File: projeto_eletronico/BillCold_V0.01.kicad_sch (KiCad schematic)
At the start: 36 parts, among them J1 USB_B, U1 ESP32-S3, U2 AMS1117, U3 W25Q128JVSIQ, X1 OSCILADOR-3225

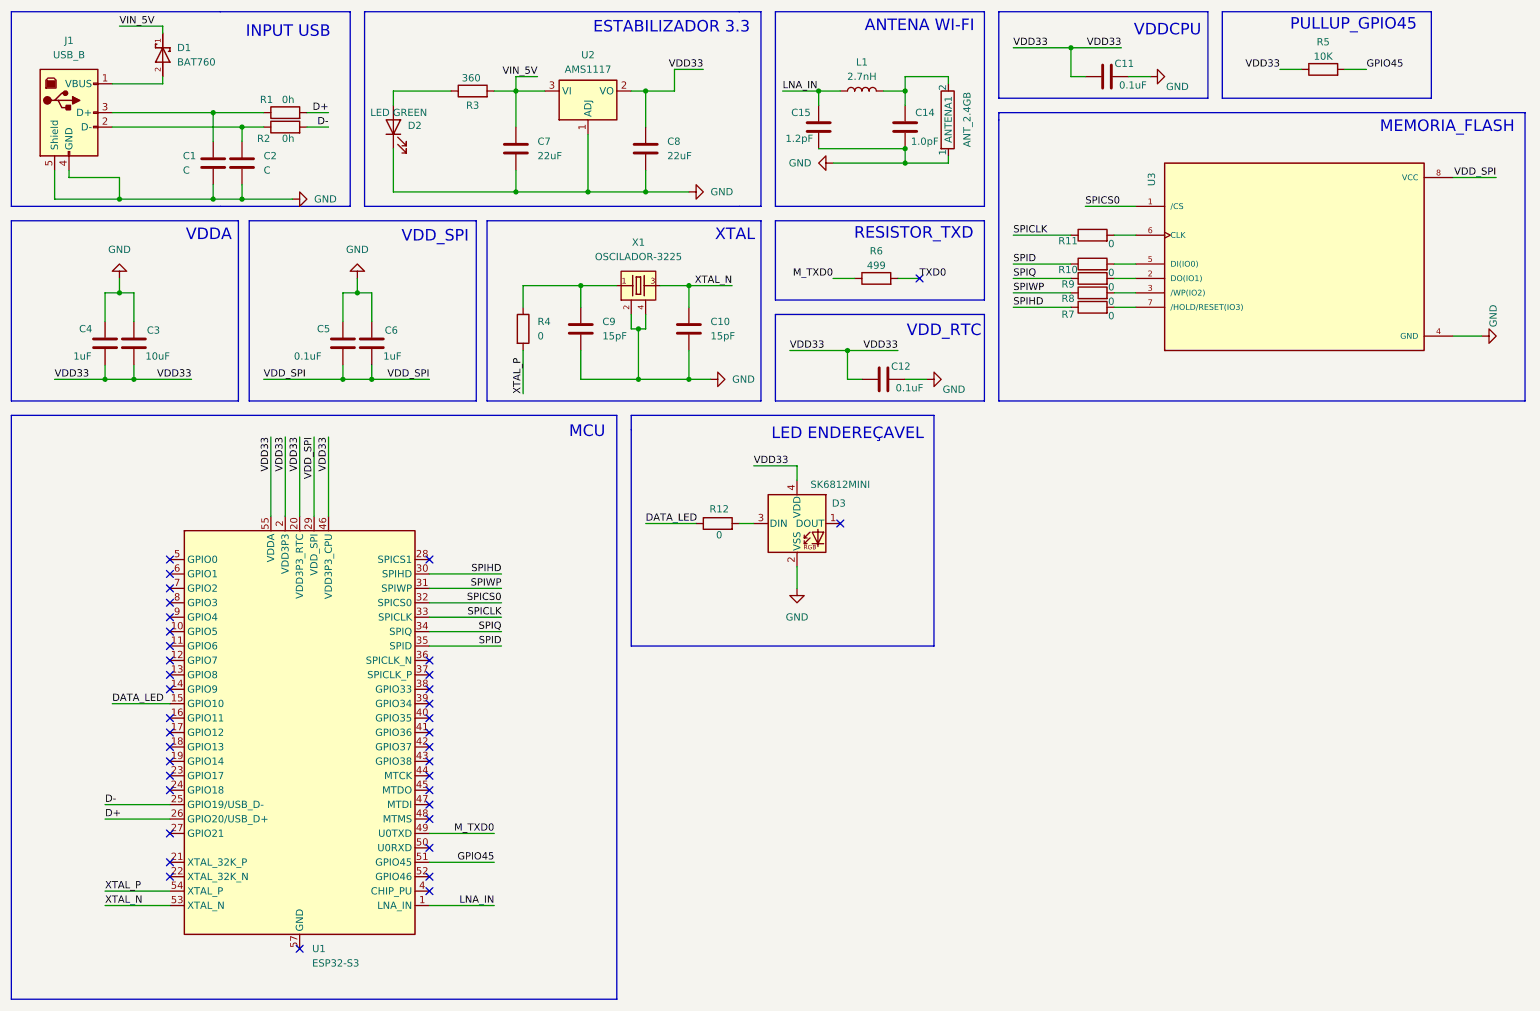
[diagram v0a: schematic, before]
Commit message: Iniciando o roteamento das trilhas da PCB
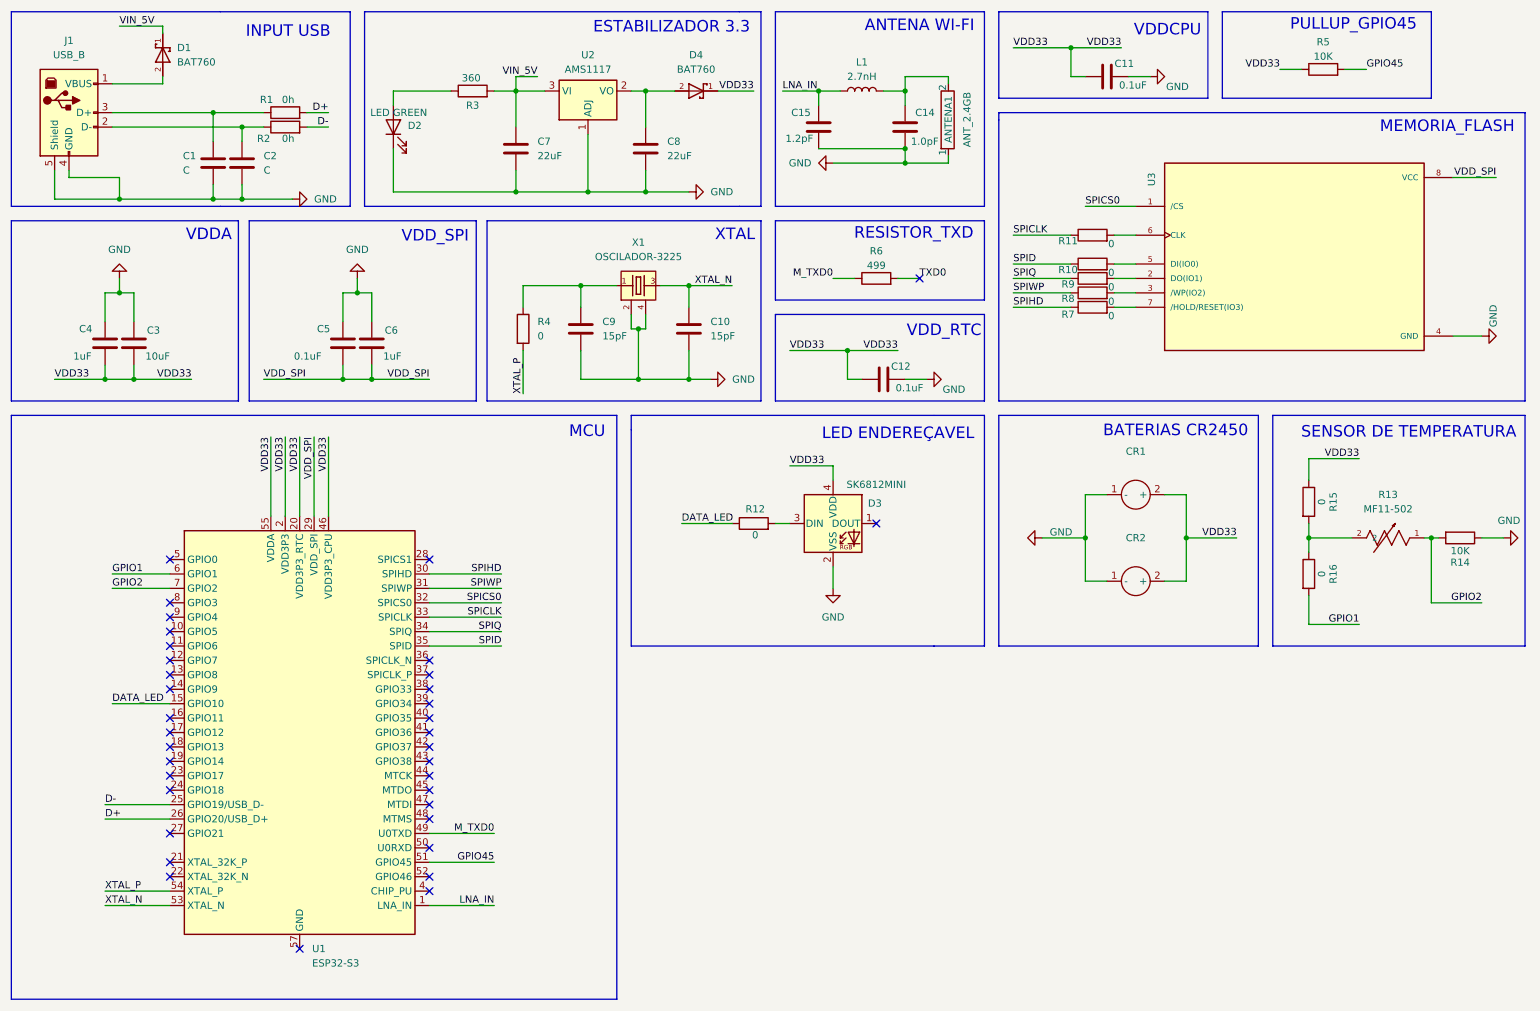
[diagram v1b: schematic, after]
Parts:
- added CR1, CR2: ~, CR2450_SUPORT:CR2450_SUPORT, symbol CR2450_SUPORT:_1
- added D4: BAT760, BAT_760:SOD323_F_, symbol BAT_760:BAT760
- added R13: MF11-502, MF11:TRES_MF52-A_CTM, symbol MF11:MF52A1103F3380
- added R14: 10K, Resistor_SMD:R_1206_3216Metric, symbol Device:R
- added R15, R16: 0, Resistor_THT:R_Axial_DIN0204_L3.6mm_D1.6mm_P5.08mm_Horizontal, symbol Device:R
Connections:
- net GND: now also CR1.1 (-), CR2.1 (-), R14.1
- net VDD33: now also CR1.2 (+), CR2.2 (+), D4.1, R15.1; no longer C8.1, U2.2 (VO)
- net GPIO1: now reaches U1.6 (GPIO1)
- net GPIO1: now also R16.2
- net GPIO2: now reaches U1.7 (GPIO2)
- net GPIO2: now also R13.1, R14.2
- new net: R13.2, R15.2, R16.1
- new net: C8.1, D4.2, U2.2 (VO)
- no-connect marks 38 -> 36
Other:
- note added: "BATERIAS CR2450"
- note added: "SENSOR DE TEMPERATURA"
- moved on the sheet: D3, R12

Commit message: Projeto finalizado
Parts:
- C1, C2: value C -> 1pF
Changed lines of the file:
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@@
 			)
 		)
-		(property "Value" "C"
+		(property "Value" "1pF"
 			(at 45.466 45.72 0)
 			(effects
@@
 			)
 		)
-		(property "Value" "C"
+		(property "Value" "1pF"
 			(at 59.69 45.7199 0)
 			(effects

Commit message: Alterando componentes smd 0603
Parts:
- added C13: 100nF, Capacitor_SMD:C_0603_1608Metric, symbol Device:C
- added R17: 0, Resistor_SMD:R_0603_1608Metric, symbol Device:R
- added R18: 10K, Resistor_SMD:R_0603_1608Metric, symbol Device:R
- added SW1: SW_Push, Button_Switch_SMD:SW_Push_1P1T_NO_E-Switch_TL3301NxxxxxG, symbol Switch:SW_Push
- added SW2: SW_SPDT_321, Button_Switch_SMD:SW_SPDT_Shouhan_MSK12C02, symbol Switch:SW_SPDT_321
- added U4: USBLC6-2SC6, Package_TO_SOT_SMD:SOT-23-6, symbol Power_Protection:USBLC6-2SC6
- C1, C11, C12, C15, C2, C3, C4, C5, C6, C7, C8: footprint Capacitor_SMD:C_1206_3216Metric -> Capacitor_SMD:C_0603_1608Metric
- C10, C9: value 15pF -> 18pF; footprint Capacitor_SMD:C_1206_3216Metric -> Capacitor_SMD:C_0603_1608Metric
- C14: footprint Inductor_SMD:L_0805_2012Metric -> Capacitor_SMD:C_0603_1608Metric
- R1, R10, R11, R12, R14, R2, R3, R4, R5, R6, R7, R8, R9: footprint Resistor_SMD:R_1206_3216Metric -> Resistor_SMD:R_0603_1608Metric
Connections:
- net D+: now also R2.2; no longer R1.2
- net D-: now also R1.2; no longer R2.2
- net GND: now also C13.1, SW1.1, U4.2 (GND)
- net VDD33: now also R18.1, SW2.3 (A); no longer CR1.2 (+), CR2.2 (+)
- net at D1.2, J1.1 (VBUS): now also U4.5 (VBUS)
- net EN: now reaches U1.4 (CHIP_PU)
- net EN: now also C13.2, R17.2, R18.2
- new net: R2.1, U4.4 (I/O2)
- new net: R1.1, U4.6 (I/O1)
- new net: R17.1, SW1.2
- new net D_N: C1.1, J1.2 (D-), U4.1 (I/O1)
- new net D_P: C2.1, J1.3 (D+), U4.3 (I/O2)
- new net VDD_BAT: CR1.2 (+), CR2.2 (+), SW2.2 (B)
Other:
- note added: "RESET"
- title: (none) -> Termokip V_1.0
- moved on the sheet: C1, C2

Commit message: Conclusão do projeto
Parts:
- removed ANTENA1: ANT_2.4GB, ANTENA_2.4GZ:Antena_2.4GB, symbol ANTENA_2.4GZ:ANT_2.4GB
- removed D3: SK6812MINI, LED_SMD:LED_SK6812MINI_PLCC4_3.5x3.5mm_P1.75mm, symbol LED:SK6812MINI
- added AE1: Antenna_Shield, RF_Antenna:Texas_SWRA117D_2.4GHz_Right, symbol Device:Antenna_Shield
- added C16: 10u, Capacitor_SMD:C_0603_1608Metric, symbol Device:C
- added C17: 1u, Capacitor_SMD:C_0603_1608Metric, symbol Device:C
- added C18, C19, C20, C21: 100n, Capacitor_SMD:C_0603_1608Metric, symbol Device:C
- added C22: 4.7u, Capacitor_SMD:C_0603_1608Metric, symbol Device:C
- added D5: SK6812, LED_SMD:LED_WS2812B-Mini_PLCC4_3.5x3.5mm, symbol LED:SK6812
- added F2: 600Ω, Inductor_SMD:L_0805_2012Metric, symbol Device:L
- added J2: Screw_Terminal_01x08, TerminalBlock:TerminalBlock_MaiXu_MX126-5.0-08P_1x08_P5.00mm, symbol Connector:Screw_Terminal_01x08
- added R19: 10k, Resistor_SMD:R_0603_1608Metric, symbol Device:R
- added R20: 470, Resistor_SMD:R_0603_1608Metric, symbol Device:R
- added R21: 10K, Resistor_SMD:R_0603_1608Metric, symbol Device:R
- added SW3: SW_Push, Button_Switch_SMD:SW_Push_1P1T_NO_E-Switch_TL3301NxxxxxG, symbol Switch:SW_Push
- added SW4: SW_Reed, Resistor_THT:R_Axial_DIN0614_L14.3mm_D5.7mm_P20.32mm_Horizontal, symbol Switch:SW_Reed
- C1, C2: value 1pF -> NC
- C11: value 0.1uF -> 1.1uF
- C12: value 0.1uF -> 100nF
- C3: value 10uF -> 1u
- C4: value 1uF -> 100nF
- C5: value 0.1uF -> 100n
- R1, R2: value 0h -> 0Ω
- R10, R11, R17, R4, R7, R8, R9: value 0 -> 0Ω
- R12: value 0 -> 360
- R6: value 499 -> 33
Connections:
- net D+: now also U4.6 (I/O1); no longer R2.2
- net D-: now also U4.4 (I/O2); no longer R1.2
- net DATA_LED: now also U1.9 (GPIO4); no longer U1.15 (GPIO10)
- net GND: now also U1.57 (GND), AE1.2 (Shield), C16.2, C17.2, C18.2, C19.2, C20.2, C21.2, C22.2, D5.1 (VSS), J2.3 (Pin_3), SW3.2, SW4.1
- net VDD33: now also C16.1, C17.1, C18.1, C20.1, D5.3 (VDD), F2.1, J2.2 (Pin_2), R19.1, R21.2; no longer U1.2 (VDD3P3), U1.3 (VDD3P3)
- net VIN_5V: now also J2.1 (Pin_1)
- net at R2.1: now also J1.3 (D+); no longer U4.4 (I/O2)
- net at D1.2, J1.1 (VBUS), U4.5 (VBUS): now also C21.1, C22.1
- net at R1.1: now also C1.1, U4.3 (I/O2); no longer U4.6 (I/O1)
- net at C14.1, L1.2: now also AE1.1 (A)
- net at R12.2: now also D5.2 (DIN)
- net GPIO5: now reaches U1.10 (GPIO5)
- net GPIO5: now also R21.1, SW4.2
- net TX_LORA: now reaches U1.23 (GPIO17)
- net TX_LORA: now also J2.4 (Pin_4)
- net RX_LORA: now reaches U1.24 (GPIO18)
- net RX_LORA: now also J2.5 (Pin_5)
- net AU_LORA: now reaches U1.27 (GPIO21)
- net AU_LORA: now also J2.8 (Pin_8)
- net M0_LORA: now reaches U1.38 (GPIO33)
- net M0_LORA: now also J2.6 (Pin_6)
- net M1_LORA: now reaches U1.39 (GPIO34)
- net M1_LORA: now also J2.7 (Pin_7)
- net BOOT: now reaches U1.5 (GPIO0)
- net BOOT: now also R19.2, R20.1
- removed net D_N: C1.1, J1.2 (D-), U4.1 (I/O1)
- removed net D_P: C2.1, J1.3 (D+), U4.3 (I/O2)
- new net: C2.1, R2.2, U4.1 (I/O1)
- new net: R20.2, SW3.1
- new net: J1.2 (D-), R1.2
- new net VDD3P3: C19.1, F2.2, U1.2 (VDD3P3), U1.3 (VDD3P3)
- no-connect marks 36 -> 28
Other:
- note added: "BOOT"
- note added: "CR1, CR2 NC"
- note added: "ON/OFF"
- note added: "R13, R15, R16 NC"
- note added: "SENS_PORT"
- note added: "SW4 NC"
- note added: "TERMINAIS"
- note added: "U3 NC"
- note added: "VAZIO"
- note added: "VDD3P3"
- title: Termokip V_1.0 -> Termokip V_0.1
- moved on the sheet: C1, C10, C2, C9, J1, R1, R12, R2, R4, SW2, U1, U4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
